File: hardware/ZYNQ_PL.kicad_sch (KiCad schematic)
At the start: 0 parts

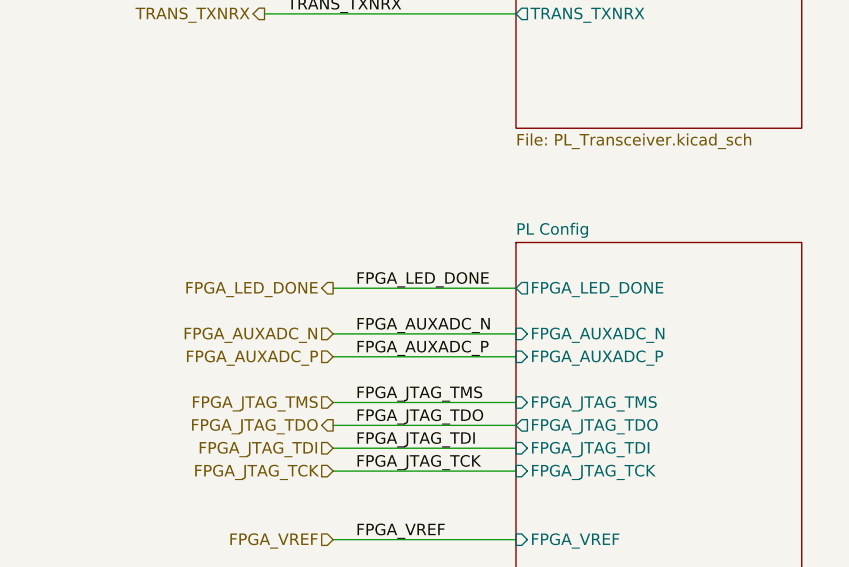
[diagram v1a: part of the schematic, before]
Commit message: Modify wrong DCDC TPS62088 package Panelize PCB Add manufacture requirements files
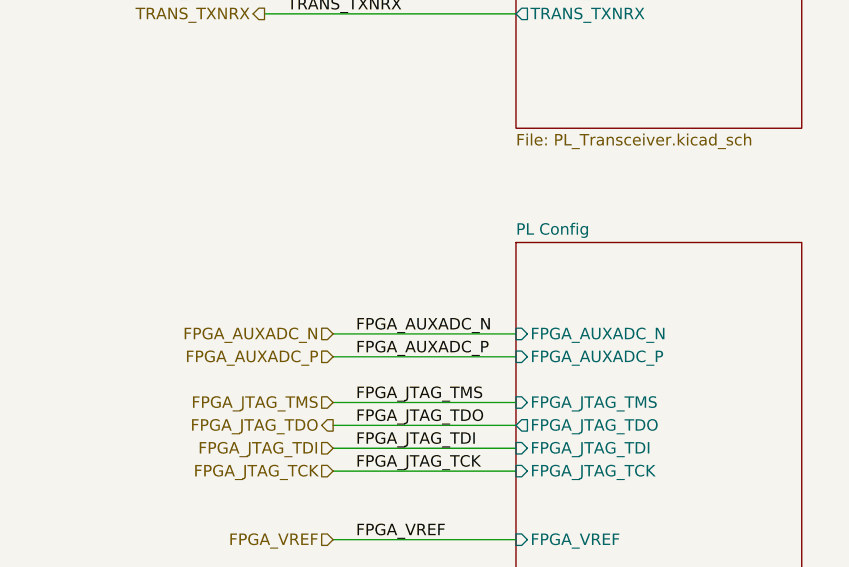
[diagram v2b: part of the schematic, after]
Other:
- sheet PL Config ports: added none; removed FPGA_LED_DONE
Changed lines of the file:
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@@
-    (stroke (width 0) (type default))
-  )
-  (wire (pts (xy 151.13 170.18) (xy 171.45 170.18))
     (stroke (width 0) (type default))
   )
@@
     (effects (font (size 1.27 1.27)) (justify left bottom))
   )
-  (label "FPGA_LED_DONE" (at 153.67 170.18 0) (fields_autoplaced)
-    (effects (font (size 1.27 1.27)) (justify left bottom))
-  )
   (label "TRANS_CTRL_IN[0..3]" (at 146.05 96.52 0) (fields_autoplaced)
     (effects (font (size 1.27 1.27)) (justify left bottom))
@@
   )
   (hierarchical_label "TRANS_ENAGC" (shape output) (at 143.51 132.08 180) (fields_autoplaced)
-    (effects (font (size 1.27 1.27)) (justify right))
-  )
-  (hierarchical_label "FPGA_LED_DONE" (shape output) (at 151.13 170.18 180) (fields_autoplaced)
     (effects (font (size 1.27 1.27)) (justify right))
   )
@@
       (effects (font (size 1.27 1.27)) (justify left))
     )
-    (pin "FPGA_LED_DONE" output (at 171.45 170.18 180)
-      (effects (font (size 1.27 1.27)) (justify left))
-    )
